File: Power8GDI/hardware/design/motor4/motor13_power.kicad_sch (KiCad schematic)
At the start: 17 parts, among them Q6200 IPD90N10S4-06, Q6201 IPD90N10S4-06, U6200 LM74800QDRRRQ1

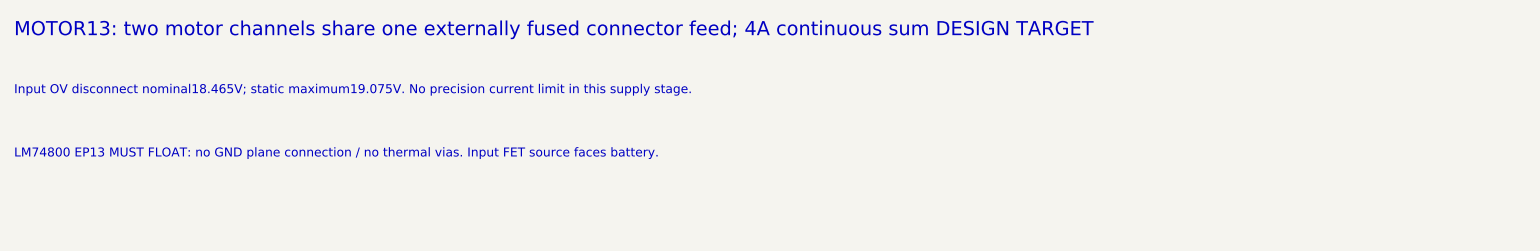
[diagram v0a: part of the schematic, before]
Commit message: Redesign sport target as six DI/PI channels with two motors and one lambda
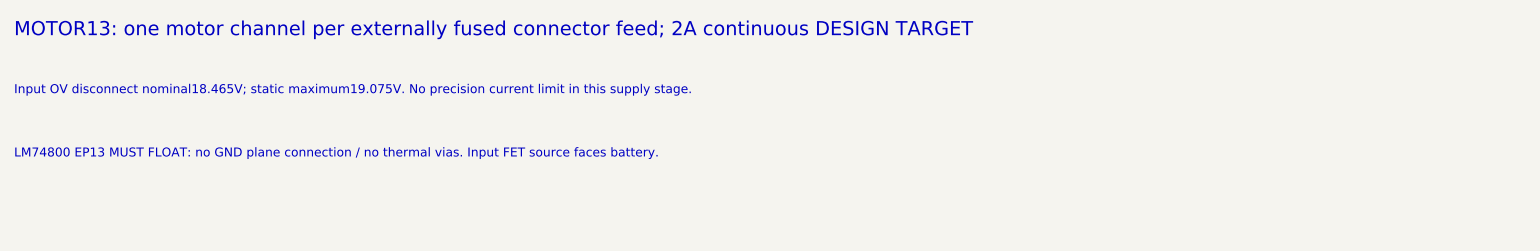
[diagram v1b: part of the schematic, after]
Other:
- note added: "MOTOR13: one motor channel per externally fused connector feed; 2A continuous DESIGN TARGET"
- note removed: "MOTOR13: two motor channels share one externally fused connector feed; 4A continuous sum DESIGN TARGET"
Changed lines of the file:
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@@
 (kicad_sch (version 20250114) (generator "eeschema") (paper "A2") (title_block (title "MOTOR13: independent protected feed") (rev "Engineering draft 0.1") (comment 1 "UNQUALIFIED: no manufacturing or engine approval"))
-(text "MOTOR13: two motor channels share one externally fused connector feed; 4A continuous sum DESIGN TARGET" (at 20 15 0) (effects (font (size 2 2)) (justify left top)))
+(text "MOTOR13: one motor channel per externally fused connector feed; 2A continuous DESIGN TARGET" (at 20 15 0) (effects (font (size 2 2)) (justify left top)))
 (text "Input OV disconnect nominal18.465V; static maximum19.075V. No precision current limit in this supply stage." (at 20 24 0) (effects (font (size 1.27 1.27)) (justify left top)))
 (text "LM74800 EP13 MUST FLOAT: no GND plane connection / no thermal vias. Input FET source faces battery." (at 20 33 0) (effects (font (size 1.27 1.27)) (justify left top)))

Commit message: Review B58 injector power stage and bind selected GDI6 BOM
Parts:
- C6200, C6201, C6202, C6203: Hardware_Qualification (none) -> BOARD_QUALIFICATION_PENDING; MPN (none) -> C0805C104K1RACTU; Manufacturer (none) -> KEMET; Procurement_Status (none) -> SELECTED_CATALOG_ITEM; Purchase_Released (none) -> false; Selection_Gaps (none) -> []; Selection_ID (none) -> SEL-50b208aec5b1; Selection_Ratings (none) -> {"capacitance_pf": 100000, "dielectric": "X7R", "rated_volt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; Selection_Source_URLs (none) -> https://www.mouser.com/datasheet/3/72/1/C0805C104K1RACTU.pdf
- C6204: Hardware_Qualification (none) -> BOARD_QUALIFICATION_PENDING; MPN (none) -> C0805C223K1RACTU; Manufacturer (none) -> KEMET; Procurement_Status (none) -> SELECTED_CATALOG_ITEM; Purchase_Released (none) -> false; Selection_Gaps (none) -> []; Selection_ID (none) -> SEL-514923e6d12b; Selection_Ratings (none) -> {"capacitance_pf": 22000, "dielectric": "X7R", "rated_volta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; Selection_Source_URLs (none) -> https://www.tme.com/Document/1eb495a6db632c9d0f71cb50aeea42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
- D6200: Hardware_Qualification (none) -> PINOUT_RATINGS_AND_DELIVERY_SUFFIX_REVIEW_PENDING; MPN (none) -> SMCJ33CA; Manufacturer (none) -> Littelfuse; Procurement_Status (none) -> REFERENCE_MPN_RETAINED; Purchase_Released (none) -> false; Selection_Gaps (none) -> ["Existing schematic MPN retained. Complete circuit rating/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; Selection_ID (none) -> SEL-57a5ac481027; Selection_Ratings (none) -> {}; Selection_Source_URLs (none) -> https://www.littelfuse.com/products/tvs-diodes/surface-moun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
- Q6200, Q6201: Hardware_Qualification (none) -> PINOUT_RATINGS_AND_DELIVERY_SUFFIX_REVIEW_PENDING; MPN (none) -> IPD90N10S406ATMA1; Manufacturer (none) -> Infineon Technologies; Procurement_Status (none) -> REFERENCE_MPN_RETAINED; Purchase_Released (none) -> false; Selection_Gaps (none) -> ["Existing schematic MPN retained. Complete circuit rating/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; Selection_ID (none) -> SEL-dc1735b932bf; Selection_Ratings (none) -> {}; Selection_Source_URLs (none) -> https://www.infineon.com/part/IPD90N10S4-06
- R6200: Hardware_Qualification (none) -> BOARD_QUALIFICATION_PENDING; MPN (none) -> RG2012P-1403-B-T5; Manufacturer (none) -> Susumu; Procurement_Status (none) -> SELECTED_CATALOG_ITEM; Purchase_Released (none) -> false; Selection_Gaps (none) -> []; Selection_ID (none) -> SEL-aca8c7a4773a; Selection_Ratings (none) -> {"aec_q200": true, "derating": "Use manufacturer power vers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; Selection_Source_URLs (none) -> https://www.digikey.com/en/products/detail/susumu/RG2012P-1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
- R6201: Hardware_Qualification (none) -> BOARD_QUALIFICATION_PENDING; MPN (none) -> RNCF0603BTE10K0; Manufacturer (none) -> Stackpole Electronics; Procurement_Status (none) -> SELECTED_CATALOG_ITEM; Purchase_Released (none) -> false; Selection_Gaps (none) -> []; Selection_ID (none) -> SEL-3a4fba6ce443; Selection_Ratings (none) -> {"aec_q200": true, "derating": "Use manufacturer power vers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; Selection_Source_URLs (none) -> https://www.digikey.com/en/products/detail/stackpole-electr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
- R6202, R6206: Hardware_Qualification (none) -> BOARD_QUALIFICATION_PENDING; MPN (none) -> CRCW06031K00FKEA; Manufacturer (none) -> Vishay; Procurement_Status (none) -> SELECTED_FAMILY_CODE; Purchase_Released (none) -> false; Selection_Gaps (none) -> []; Selection_ID (none) -> SEL-38197231a947; Selection_Ratings (none) -> {"aec_q200": true, "derating": "Use manufacturer power vers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; Selection_Source_URLs (none) -> https://www.vishay.com/docs/20035/dcrcwe3.pdf
- R6203, R6207: Hardware_Qualification (none) -> BOARD_QUALIFICATION_PENDING; MPN (none) -> CRCW060310K0FKEA; Manufacturer (none) -> Vishay; Procurement_Status (none) -> SELECTED_FAMILY_CODE; Purchase_Released (none) -> false; Selection_Gaps (none) -> []; Selection_ID (none) -> SEL-9c0806476875; Selection_Ratings (none) -> {"aec_q200": true, "derating": "Use manufacturer power vers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; Selection_Source_URLs (none) -> https://www.vishay.com/docs/20035/dcrcwe3.pdf
- R6204, R6205: Hardware_Qualification (none) -> BOARD_QUALIFICATION_PENDING; MPN (none) -> CRCW06031M00FKEA; Manufacturer (none) -> Vishay; Procurement_Status (none) -> SELECTED_FAMILY_CODE; Purchase_Released (none) -> false; Selection_Gaps (none) -> []; Selection_ID (none) -> SEL-0d98ae3ae719; Selection_Ratings (none) -> {"aec_q200": true, "derating": "Use manufacturer power vers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; Selection_Source_URLs (none) -> https://www.vishay.com/docs/20035/dcrcwe3.pdf
- U6200: Hardware_Qualification (none) -> BOARD_STRESS_AND_LAYOUT_REVIEW_REQUIRED; MPN (none) -> LM74800QDRRRQ1; Manufacturer (none) -> Texas Instruments; Procurement_Status (none) -> SELECTED_CONDITIONAL; Purchase_Released (none) -> false; Selection_Gaps (none) -> ["Catalog family limits verified; exact order suffix and ci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; Selection_ID (none) -> SEL-9eef1a739cc4; Selection_Ratings (none) -> {"reverse_input_v": -65, "supply_max_v": 65, "supply_min_v"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; Selection_Source_URLs (none) -> https://www.ti.com/product/LM7480-Q1
